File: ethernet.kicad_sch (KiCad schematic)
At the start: 50 parts, among them U7 LAN8720A, U8 ARJM11C7-114-BA-EW2, Y1 25MHz

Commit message: Ethernet routing
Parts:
- added R146, R147: 4.7k, Resistor_SMD:R_0402_1005Metric, symbol SparkFun-Resistor:R
- R120, R121, R122, R123, R124, R125, R126, R127, R128, R129, R130, R131, R132, R133, R134, R135, R136, R137, R138, R139, R140, R141, R142, R143, R144: footprint Capacitor_SMD:C_0402_1005Metric -> Resistor_SMD:R_0402_1005Metric
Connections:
- net GND: now also R146.1, R147.1
- net LED1: now also R147.2
- net LED2: now also R146.2
- net VDDCR: now reaches C62.1, C63.1, U7.6 (VDDCR)

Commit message: Routing
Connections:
- net REFCLKO renamed INTn
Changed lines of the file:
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@@
-	(wire
-		(pts
-			(xy 72.39 101.6) (xy 86.36 101.6)
-		)
-		(stroke
-			(width 0)
-			(type default)
-		)
-	)
 	(wire
 		(pts
@@
 		(pts
 			(xy 44.45 130.81) (xy 44.45 135.89)
+		)
+		(stroke
+			(width 0)
+			(type default)
+		)
+	)
+	(wire
+		(pts
+			(xy 66.04 101.6) (xy 86.36 101.6)
 		)
 		(stroke
@@
 		(fields_autoplaced yes)
 		(effects
+			(font
+				(size 1.27 1.27)
+			)
+			(justify right)
+		)
+	)
+	(hierarchical_label "INTn"
+		(shape output)
+		(at 66.04 101.6 180)
+		(fields_autoplaced yes)
+		(effects

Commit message: Started an entire reroute
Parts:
- Y1: footprint SparkFun-Clock:Crystal_SMD_2.0x1.6mm -> Crystal:Crystal_SMD_2016-4Pin_2.0x1.6mm
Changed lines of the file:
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@@
 (kicad_sch
-	(version 20231120)
+	(version 20250114)
 	(generator "eeschema")
-	(generator_version "8.0")
+	(generator_version "9.0")
 	(paper "A4")
+	(rectangle
+		(start 153.67 72.39)
+		(end 204.47 111.76)
+		(stroke
+			(width 0)
+			(type dash)
+			(color 255 255 0 1)
+		)
+		(fill
+			(type none)
+		)
+	)
+	(text "Probably not needed, remove later if not"
+		(exclude_from_sim no)
+		(at 178.816 74.168 0)
+		(effects
+			(font
+				(size 1.27 1.27)
+				(color 255 255 0 1)
+			)
+		)
+	)
 	(junction
 		(at 158.75 50.8)
@@
 		)
 	)
-	(rectangle
-		(start 153.67 72.39)
-		(end 204.47 111.76)
-		(stroke
-			(width 0)
-			(type dash)
-			(color 255 255 0 1)
-		)
-		(fill
-			(type none)
-		)
-	)
-	(text "Probably not needed, remove later if not"
-		(exclude_from_sim no)
-		(at 178.816 74.168 0)
-		(effects
-			(font
-				(size 1.27 1.27)
-				(color 255 255 0 1)
-			)
-		)
-	)
 	(label "VDD"
 		(at 115.57 154.94 180)
-		(fields_autoplaced yes)
 		(effects
 			(font
@@
 	(label "LED2"
 		(at 261.62 127 180)
-		(fields_autoplaced yes)
 		(effects
 			(font
@@
 	(label "GREEN"
 		(at 240.03 72.39 180)
-		(fields_autoplaced yes)
 		(effects
 			(font
@@
 	(label "RXP"
 		(at 128.27 81.28 180)
-		(fields_autoplaced yes)
 		(effects
 			(font
@@
 	(label "PHYADDR"
 		(at 25.4 175.26 0)
-		(fields_autoplaced yes)
 		(effects
 			(font
@@
 	(label "LED1"
 		(at 261.62 121.92 180)
-		(fields_autoplaced yes)
 		(effects
 			(font
@@
 	(label "YELLOW"
 		(at 261.62 124.46 180)
-		(fields_autoplaced yes)
 		(effects
 			(font
@@
 	(label "REFCLKO"
 		(at 138.43 168.91 180)
-		(fields_autoplaced yes)
 		(effects
 			(font
@@
 	(label "LED2"
 		(at 132.08 99.06 180)
-		(fields_autoplaced yes)
 		(effects
 			(font
@@
 	(label "RXN"
 		(at 185.42 124.46 0)
-		(fields_autoplaced yes)
 		(effects
 			(font
@@
 	(label "MODE2"
 		(at 72.39 88.9 0)
-		(fields_autoplaced yes)
 		(effects
 			(font
@@
 	(label "MODE1"
 		(at 72.39 83.82 0)
-		(fields_autoplaced yes)
 		(effects
 			(font
@@
 	(label "TXN"
 		(at 269.24 31.75 180)
-		(fields_autoplaced yes)
 		(effects
 			(font
@@
 	(label "LED1"
 		(at 134.62 96.52 180)
-		(fields_autoplaced yes)
 		(effects
 			(font
@@
 	(label "VDDCR"
 		(at 85.09 34.29 0)
-		(fields_autoplaced yes)
 		(effects
 			(font
@@
 	(label "VDD"
 		(at 58.42 152.4 0)
-		(fields_autoplaced yes)
 		(effects
 			(font
@@
 	(label "RXP"
 		(at 185.42 129.54 0)
-		(fields_autoplaced yes)
 		(effects
 			(font
@@
 	(label "RXP"
 		(at 208.28 36.83 0)
-		(fields_autoplaced yes)
 		(effects
 			(font
@@
 	(label "VDDA"
 		(at 109.22 29.21 0)
-		(fields_autoplaced yes)
 		(effects
 			(font
@@
 	(label "TXP"
 		(at 264.16 129.54 180)
-		(fields_autoplaced yes)
 		(effects
 			(font
@@
 	(label "MODE0"
 		(at 25.4 167.64 0)
-		(fields_autoplaced yes)
 		(effects
 			(font
@@
 	(label "RXN"
 		(at 269.24 36.83 180)
-		(fields_autoplaced yes)
 		(effects
 			(font
@@
 	(label "MODE2"
 		(at 25.4 172.72 0)
-		(fields_autoplaced yes)
 		(effects
 			(font
@@
 	(label "VDD"
 		(at 269.24 34.29 180)
-		(fields_autoplaced yes)
 		(effects
 			(font
@@
 	(label "TXN"
 		(at 264.16 134.62 180)
-		(fields_autoplaced yes)
 		(effects
 			(font
@@
 	(label "GREEN"
 		(at 261.62 119.38 180)
-		(fields_autoplaced yes)
 		(effects
 			(font
@@
 	(label "PHYADDR"
 		(at 72.39 86.36 0)
-		(fields_autoplaced yes)
 		(effects
 			(font
@@
 	(label "TXP"
 		(at 208.28 31.75 0)
-		(fields_autoplaced yes)
 		(effects
 			(font
@@
 	(label "MODE0"
 		(at 72.39 81.28 0)
-		(fields_autoplaced yes)
 		(effects
 			(font
@@
 	(label "TXN"
 		(at 128.27 78.74 180)
-		(fields_autoplaced yes)
 		(effects
 			(font
@@
 	(label "REFCLKO"
 		(at 72.39 101.6 0)
-		(fields_autoplaced yes)
 		(effects
 			(font
@@
 	(label "YELLOW"
 		(at 255.27 72.39 180)
-		(fields_autoplaced yes)
 		(effects
 			(font
@@
 	(label "TXP"
 		(at 128.27 76.2 180)
-		(fields_autoplaced yes)
 		(effects
 			(font
@@
 	(label "VDD"
 		(at 40.64 29.21 0)
-		(fields_autoplaced yes)
 		(effects
 			(font
@@
 	(label "MODE1"
 		(at 25.4 170.18 0)
-		(fields_autoplaced yes)
 		(effects
 			(font
@@
 	(label "RXN"
 		(at 128.27 83.82 180)
-		(fields_autoplaced yes)
 		(effects
 			(font
@@
 		(shape input)
 		(at 66.04 93.98 180)
-		(fields_autoplaced yes)
 		(effects
 			(font
@@
 		(shape input)
 		(at 66.04 73.66 180)
-		(fields_autoplaced yes)
 		(effects
 			(font
@@
 		(shape output)
 		(at 66.04 83.82 180)
-		(fields_autoplaced yes)
 		(effects
 			(font
@@
 		(shape input)
 		(at 66.04 91.44 180)
-		(fields_autoplaced yes)
 		(effects
 			(font
@@
 		(shape output)
 		(at 66.04 101.6 180)
-		(fields_autoplaced yes)
 		(effects
 			(font
@@
 		(shape input)
 		(at 66.04 76.2 180)
-		(fields_autoplaced yes)
 		(effects
 			(font
@@
 		(shape output)
 		(at 66.04 88.9 180)
-		(fields_autoplaced yes)
 		(effects
 			(font
@@
 		(shape output)
 		(at 101.6 168.91 180)
-		(fields_autoplaced yes)
 		(effects
 			(font
@@
 		(shape output)
 		(at 66.04 81.28 180)
-		(fields_autoplaced yes)
 		(effects
 			(font
@@
 		(shape input)
 		(at 43.18 109.22 180)
-		(fields_autoplaced yes)
 		(effects
 			(font
@@
 		(shape input)
 		(at 66.04 78.74 180)
-		(fields_autoplaced yes)
 		(effects
 			(font
@@
 		(shape input)
 		(at 27.94 29.21 180)
-		(fields_autoplaced yes)
 		(effects
 			(font
@@
 		(shape input)
 		(at 66.04 99.06 180)
-		(fields_autoplaced yes)
 		(effects
 			(font
@@
 			)
 		)
-		(property "Footprint" "SparkFun-Clock:Crystal_SMD_2.0x1.6mm"
+		(property "Footprint" "Crystal:Crystal_SMD_2016-4Pin_2.0x1.6mm"
 			(at 72.39 128.27 0)
 			(effects

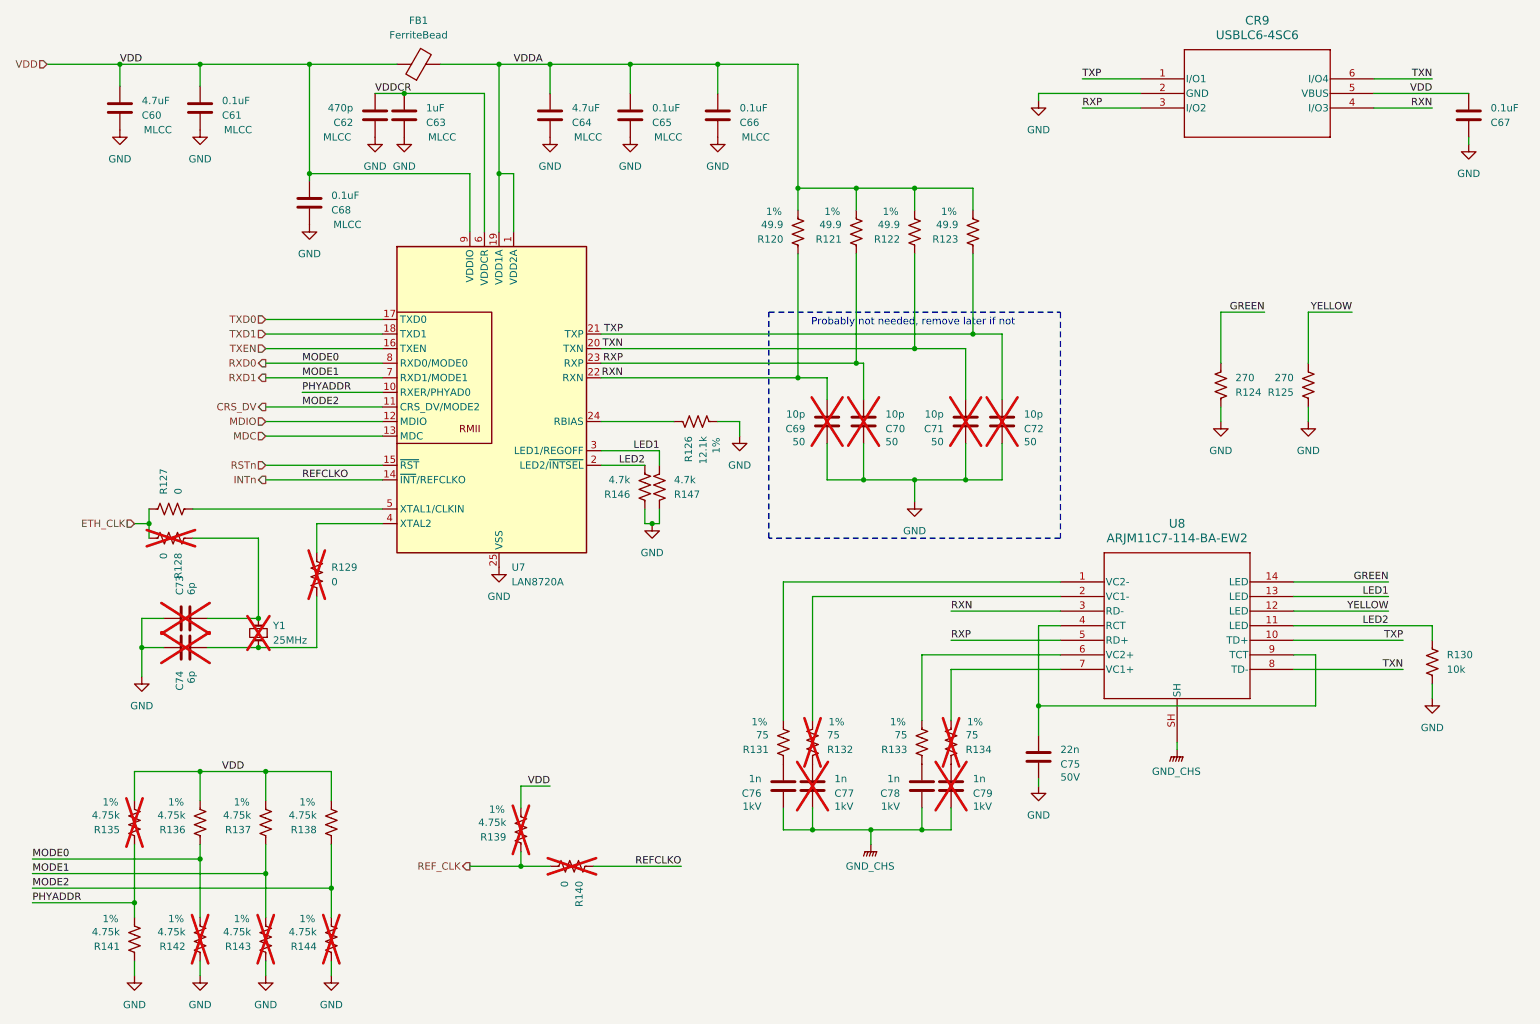
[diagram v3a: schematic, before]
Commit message: Routing ethernet
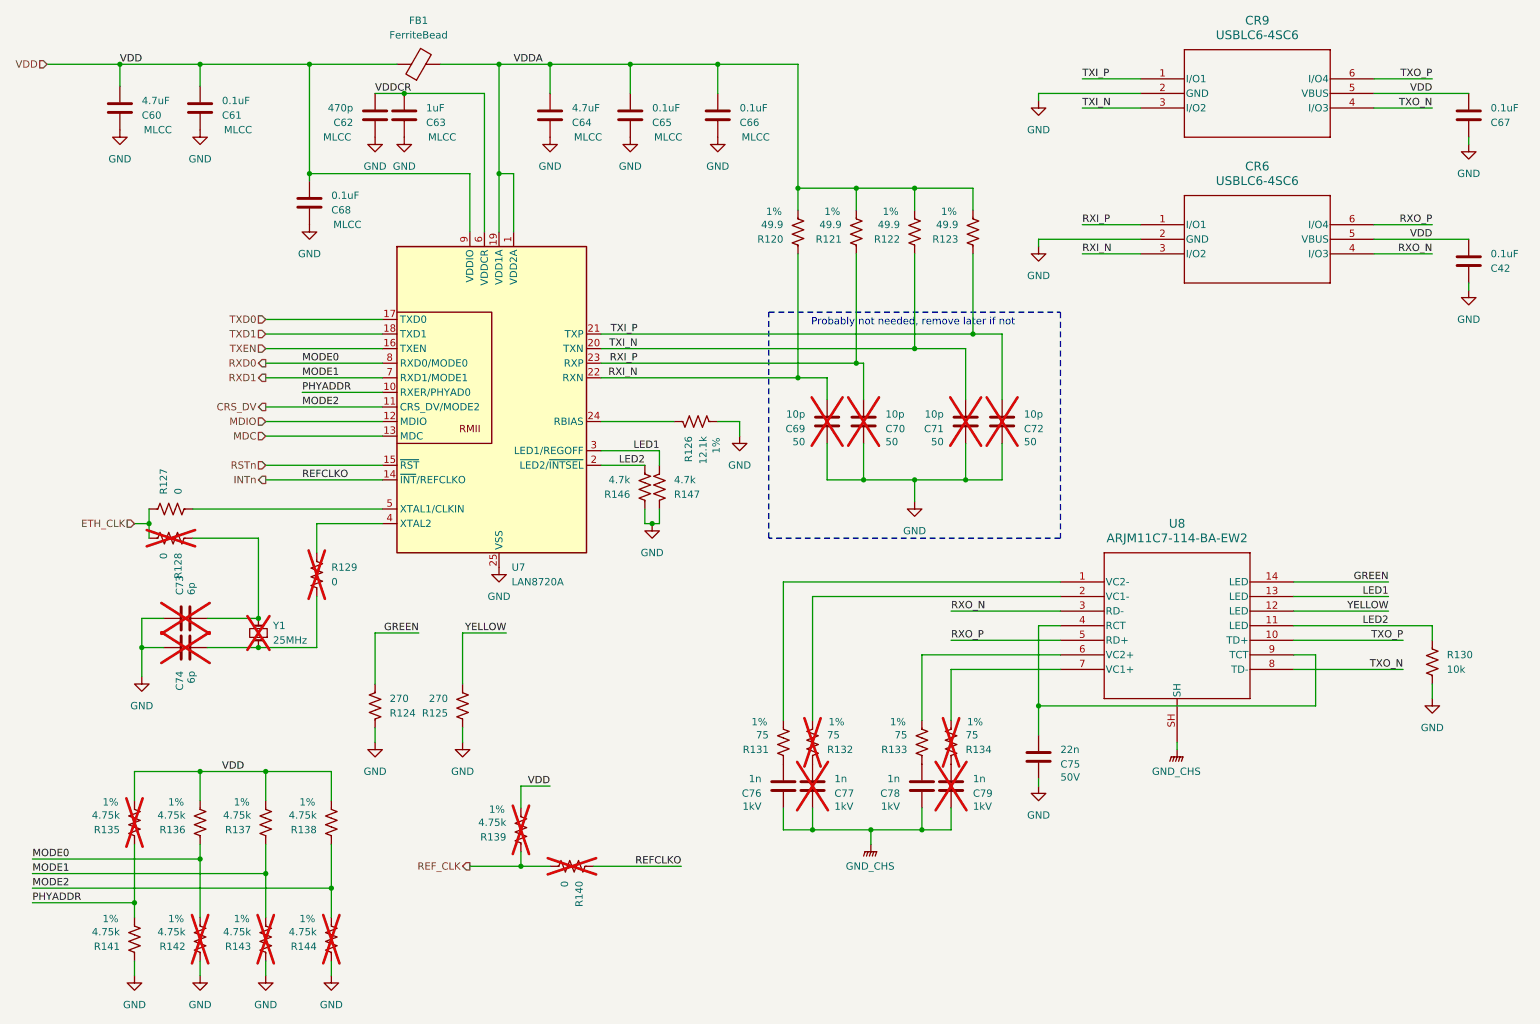
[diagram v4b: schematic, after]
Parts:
- added C42: 0.1uF, Capacitor_SMD:C_0402_1005Metric, symbol SparkFun-Capacitor:C
- added CR6: USBLC6-4SC6, footprints:SOT23-6L_STM, symbol USBLC6_4SC6:USBLC6-4SC6
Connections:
- net GND: now also C42.2, CR6.2 (GND)
- net VDD: now also C42.1, CR6.5 (VBUS)
- net RXN renamed RXI_N
- net RXI_N: now also CR6.3 (I/O2); no longer CR9.4 (I/O3), U8.3 (RD-)
- net RXP renamed RXI_P
- net RXI_P: now also CR6.1 (I/O1); no longer CR9.3 (I/O2), U8.5 (RD+)
- net TXN renamed TXI_N
- net TXI_N: now also CR9.3 (I/O2); no longer CR9.6 (I/O4), U8.8 (TD-)
- net TXP renamed TXI_P
- net TXI_P: no longer U8.10 (TD+)
- new net RXO_N: CR6.4 (I/O3), U8.3 (RD-)
- new net RXO_P: CR6.6 (I/O4), U8.5 (RD+)
- new net TXO_N: CR9.4 (I/O3), U8.8 (TD-)
- new net TXO_P: CR9.6 (I/O4), U8.10 (TD+)
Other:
- moved on the sheet: R124, R125

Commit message: Routing Eth
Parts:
- removed C69, C70, C71, C72: 10p, Capacitor_SMD:C_0402_1005Metric, symbol SparkFun-Capacitor:C
- removed R127, R128, R129, R140: 0, Resistor_SMD:R_0402_1005Metric, symbol SparkFun-Resistor:R
- removed R135, R139, R142, R143, R144: 4.75k, Resistor_SMD:R_0402_1005Metric, symbol SparkFun-Resistor:R
- removed R146, R147: 4.7k, Resistor_SMD:R_0402_1005Metric, symbol SparkFun-Resistor:R
- removed Y1: 25MHz, Crystal:Crystal_SMD_2016-4Pin_2.0x1.6mm, symbol SparkFun-Clock:Crystal_25MHz_2.0x1.6mm
- added R31: 10k, Resistor_SMD:R_0402_1005Metric, symbol SparkFun-Resistor:R
- added Y2: Crystal_GND24, Crystal:Crystal_SMD_Abracon_ABM8G-4Pin_3.2x2.5mm, symbol Device:Crystal_GND24
- C73, C74: value 6p -> 18p; now fitted
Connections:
- net GND: now also C73.2, Y2.2, Y2.4; no longer C73.1
- net INTn: now also R31.1
- net VDD: now also R31.2
- net at U7.5 (XTAL1/CLKIN): now also C73.1, Y2.1
- net at C74.2: now also U7.4 (XTAL2), Y2.3
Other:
- note removed: "Probably not needed, remove later if not"

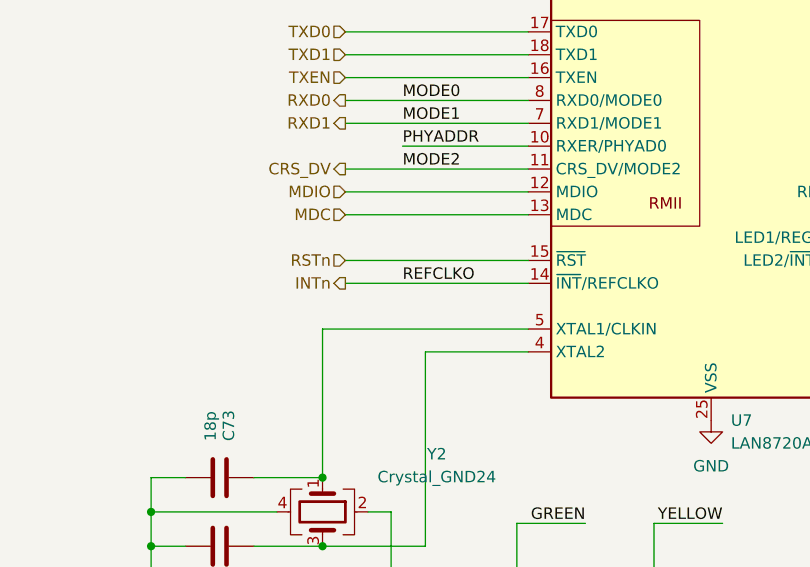
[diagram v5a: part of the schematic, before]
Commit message: Routing power and fixing minor things
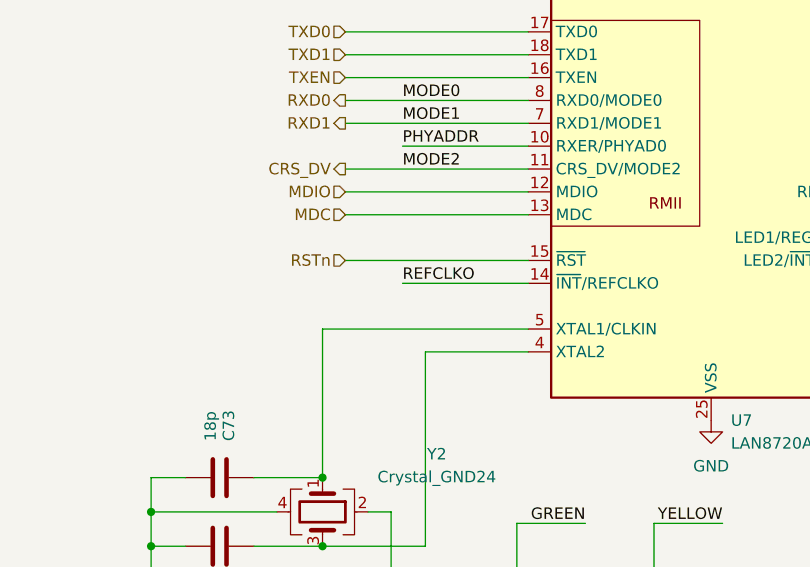
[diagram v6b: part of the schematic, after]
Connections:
- net INTn renamed REF_CLK
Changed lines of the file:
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@@
 	(wire
 		(pts
-			(xy 66.04 101.6) (xy 86.36 101.6)
+			(xy 72.39 101.6) (xy 86.36 101.6)
 		)
 		(stroke
@@
 		(effects
 			(font
-				(size 1.27 1.27)
-			)
-			(justify right)
-		)
-	)
-	(hierarchical_label "INTn"
-		(shape output)
-		(at 66.04 101.6 180)
-		(effects
-			(font
